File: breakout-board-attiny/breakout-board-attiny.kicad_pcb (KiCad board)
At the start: 2 copper layers, 36 x 21.5 mm, 6 parts, among them J1 Conn_01x07_Male, J2 Conn_01x07_Male, U1 ATtiny424-X

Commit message: ATtiny breakout board done
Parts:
- added D2: LED_Small, Diode_SMD:D_1206_3216Metric, F.Cu at (139.4, 97.0)
- added R1: 330, Resistor_SMD:R_1206_3216Metric, F.Cu at (139.5, 100.3)
- moved J1 0.28 mm to (146.8, 112.8)
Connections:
- net /PA1 renamed /TXD/PA1
- net /PA2 renamed /RXD/PA2
- net /PA3 renamed /XCK/PA3
- net /PA4 renamed /XDIR/PA4
- net /TX/~{RX}/PB0 renamed /SCL/XDIR/PB0
- net /XCK/PB1 renamed /SDA/XCK/PB1
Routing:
- net Net-(D2-A): track 0.00 -> 3.34 mm
- net /TxD/PB2: track 8.17 -> 11.5 mm
- added copper zone on F.Cu, net GND
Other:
- board size 36 x 21.5 mm -> 40.6 x 21.5 mm
- board text added: "PA1/TXD1"
- board text added: "PA2/RXD1"
- board text added: "PA3/XCK1"
- board text added: "PB0/XDIR0/SCL"
- board text added: "PB1/XCK0/SDA"
- board text added: "RXD0/PB3"
- board text added: "TXD0/PB2"
- board text added: "XDIR1/PA4"
- board text removed: "PA1"
- board text removed: "PA2"
- board text removed: "PA3"
- board text removed: "PA4"
- board text removed: "PB0/TX/RX"
- board text removed: "PB1/XCK"
- board text removed: "PB2/TxD"
- board text removed: "PB3/RxD"

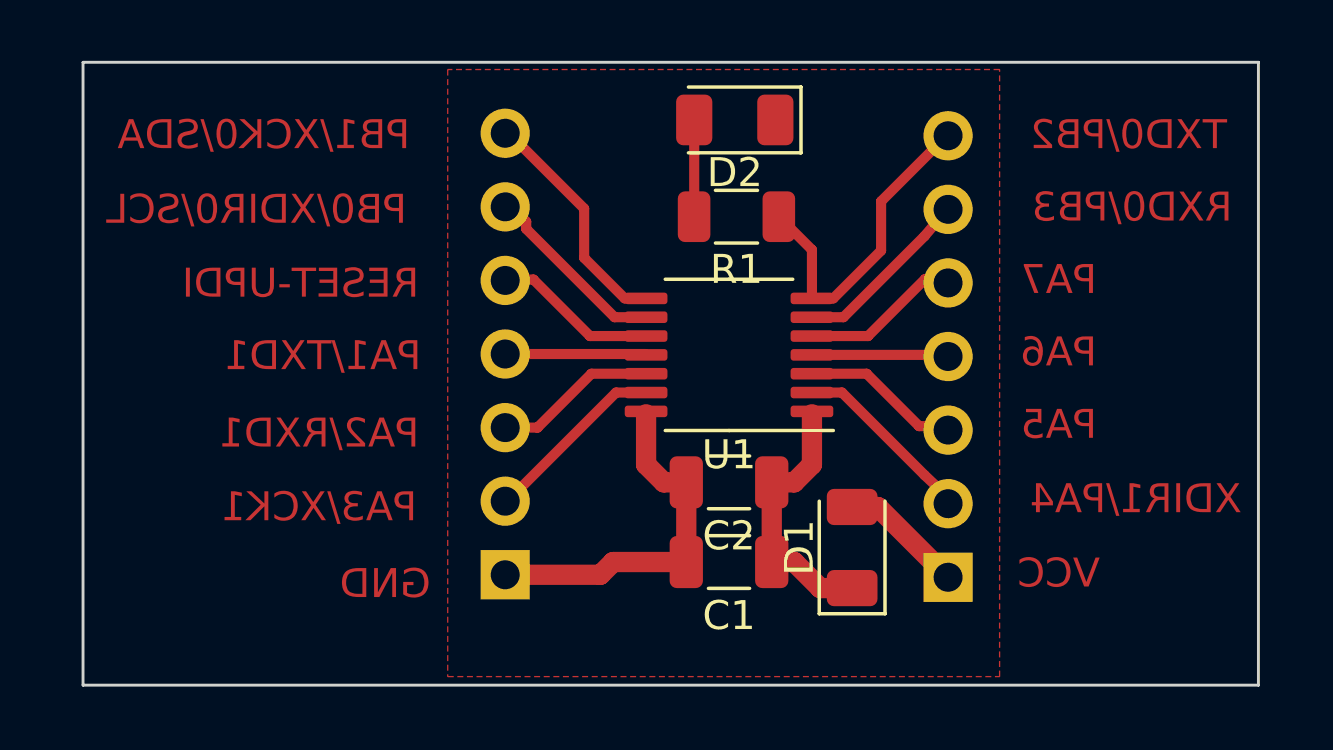
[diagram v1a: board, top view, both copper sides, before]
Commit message: ATtiny breakout board finished and ready for production
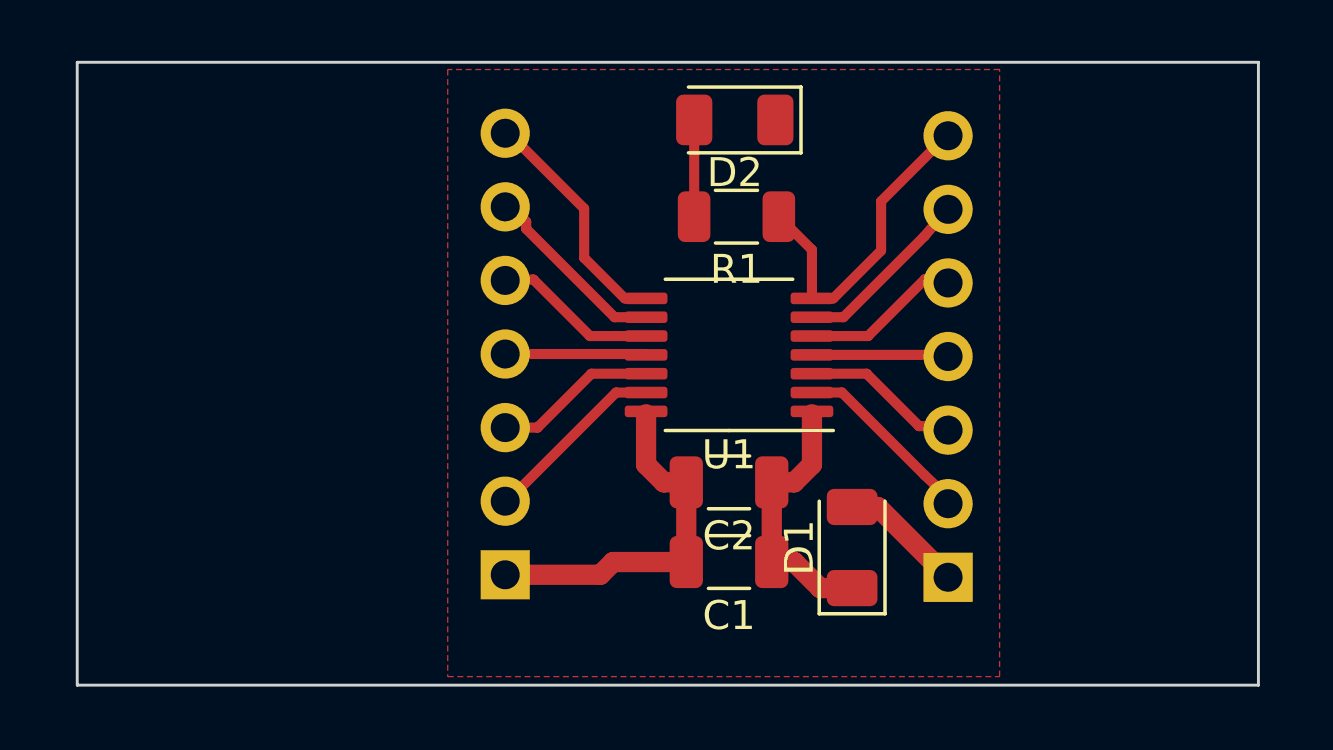
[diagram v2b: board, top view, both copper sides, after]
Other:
- board size 40.6 x 21.5 mm -> 40.8 x 21.5 mm
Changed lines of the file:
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@@
     )
   )
-  (gr_rect (start 116.952 95) (end 157.524 116.5)
+  (gr_rect (start 116.752 95) (end 157.524 116.5)
     (stroke (width 0.1) (type solid)) (fill none) (layer "Edge.Cuts"))
-  (gr_text "PA6" (at 150.627 105) (layer "F.Cu")
+  (gr_text "PA6" (at 150.627 105) (layer "B.SilkS")
     (effects (font (size 1 1) (thickness 0.15)) (justify mirror))
   )
-  (gr_text "XDIR1/PA4" (at 153.289 110.066869) (layer "F.Cu")
+  (gr_text "XDIR1/PA4" (at 153.289 110.066869) (layer "B.SilkS")
     (effects (font (size 1 1) (thickness 0.15)) (justify mirror))
   )
-  (gr_text "VCC" (at 150.627642 112.632373) (layer "F.Cu")
+  (gr_text "VCC" (at 150.627642 112.632373) (layer "B.SilkS")
     (effects (font (size 1 1) (thickness 0.15)) (justify mirror))
   )
-  (gr_text "PA7" (at 150.627 102.5) (layer "F.Cu")
+  (gr_text "PA7" (at 150.627 102.5) (layer "B.SilkS")
     (effects (font (size 1 1) (thickness 0.15)) (justify mirror))
   )
-  (gr_text "PB0/XDIR0/SCL" (at 122.936 100.076) (layer "F.Cu")
+  (gr_text "PB0/XDIR0/SCL" (at 122.936 100.076) (layer "B.SilkS")
     (effects (font (size 1 1) (thickness 0.15)) (justify mirror))
   )
-  (gr_text "PA2/RXD1" (at 125.095 107.800674) (layer "F.Cu")
+  (gr_text "PA2/RXD1" (at 125.095 107.800674) (layer "B.SilkS")
     (effects (font (size 1 1) (thickness 0.15)) (justify mirror))
   )
-  (gr_text "TXD0/PB2" (at 153.035 97.5) (layer "F.Cu")
+  (gr_text "TXD0/PB2" (at 153.035 97.5) (layer "B.SilkS")
     (effects (font (size 1 1) (thickness 0.15)) (justify mirror))
   )
-  (gr_text "PA3/XCK1" (at 125.095 110.344799) (layer "F.Cu")
+  (gr_text "PA3/XCK1" (at 125.095 110.344799) (layer "B.SilkS")
     (effects (font (size 1 1) (thickness 0.15)) (justify mirror))
   )
-  (gr_text "PB1/XCK0/SDA" (at 123.19 97.5) (layer "F.Cu")
+  (gr_text "PB1/XCK0/SDA" (at 123.19 97.5) (layer "B.SilkS")
     (effects (font (size 1 1) (thickness 0.15)) (justify mirror))
   )
-  (gr_text "PA1/TXD1\n" (at 125.222 105.128275) (layer "F.Cu")
+  (gr_text "PA1/TXD1\n" (at 125.222 105.128275) (layer "B.SilkS")
     (effects (font (size 1 1) (thickness 0.15)) (justify mirror))
   )
-  (gr_text "PA5" (at 150.627 107.5) (layer "F.Cu")
+  (gr_text "PA5" (at 150.627 107.5) (layer "B.SilkS")
     (effects (font (size 1 1) (thickness 0.15)) (justify mirror))
   )
-  (gr_text "RXD0/PB3" (at 153.162 100) (layer "F.Cu")
+  (gr_text "RXD0/PB3" (at 153.162 100) (layer "B.SilkS")
     (effects (font (size 1 1) (thickness 0.15)) (justify mirror))
   )
-  (gr_text "RESET-UPDI" (at 124.46 102.626909) (layer "F.Cu")
+  (gr_text "RESET-UPDI" (at 124.46 102.626909) (layer "B.SilkS")
     (effects (font (size 1 1) (thickness 0.15)) (justify mirror))
   )
-  (gr_text "GND" (at 127.381 112.995819) (layer "F.Cu")
+  (gr_text "GND" (at 127.381 112.995819) (layer "B.SilkS")
     (effects (font (size 1 1) (thickness 0.15)) (justify mirror))
   )

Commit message: ...
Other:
- board size 40.8 x 21.5 mm -> 19 x 19.3 mm
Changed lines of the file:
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@@
     (pad_to_mask_clearance 0)
     (pcbplotparams
-      (layerselection 0x00010fc_ffffffff)
+      (layerselection 0x0001000_7fffffff)
       (plot_on_all_layers_selection 0x0000000_00000000)
       (disableapertmacros false)
@@
       (outputformat 1)
       (mirror false)
-      (drillshape 1)
+      (drillshape 0)
       (scaleselection 1)
-      (outputdirectory "")
+      (outputdirectory "plot/")
     )
   )
@@
     (fp_line (start 1.6 0.8) (end -1.6 0.8)
       (stroke (width 0.1) (type solid)) (layer "F.Fab"))
-    (pad "1" smd roundrect (at -1.475 0 180) (size 1.15 1.8) (layers "F.Cu" "F.Paste" "F.Mask") (roundrect_rratio 0.217391)
+    (pad "1" smd roundrect (at -1.475 0 180) (size 1.15 1.8) (layers "F.Cu" "F.Paste" "F.Mask") (roundrect_rratio 0.2173913043)
       (net 1 "/sVCC") (pintype "passive"))
-    (pad "2" smd roundrect (at 1.475 0 180) (size 1.15 1.8) (layers "F.Cu" "F.Paste" "F.Mask") (roundrect_rratio 0.217391)
+    (pad "2" smd roundrect (at 1.475 0 180) (size 1.15 1.8) (layers "F.Cu" "F.Paste" "F.Mask") (roundrect_rratio 0.2173913043)
       (net 2 "GND") (pintype "passive"))
     (model "${KICAD6_3DMODEL_DIR}/Capacitor_SMD.3dshapes/C_1206_3216Metric.wrl"
@@
     (fp_line (start 1.6 0.8) (end -1.6 0.8)
       (stroke (width 0.1) (type solid)) (layer "F.Fab"))
-    (pad "1" smd roundrect (at -1.4625 0 180) (size 1.125 1.75) (layers "F.Cu" "F.Paste" "F.Mask") (roundrect_rratio 0.222222)
+    (pad "1" smd roundrect (at -1.4625 0 180) (size 1.125 1.75) (layers "F.Cu" "F.Paste" "F.Mask") (roundrect_rratio 0.2222222222)
       (net 5 "/TxD{slash}PB2") (pintype "passive"))
-    (pad "2" smd roundrect (at 1.4625 0 180) (size 1.125 1.75) (layers "F.Cu" "F.Paste" "F.Mask") (roundrect_rratio 0.222222)
+    (pad "2" smd roundrect (at 1.4625 0 180) (size 1.125 1.75) (layers "F.Cu" "F.Paste" "F.Mask") (roundrect_rratio 0.2222222222)
       (net 16 "Net-(D2-A)") (pintype "passive"))
     (model "${KICAD6_3DMODEL_DIR}/Resistor_SMD.3dshapes/R_1206_3216Metric.wrl"
@@
     (fp_line (start 1.6 0.8) (end -1.6 0.8)
       (stroke (width 0.1) (type solid)) (layer "F.Fab"))
-    (pad "1" smd roundrect (at -1.475 0 180) (size 1.15 1.8) (layers "F.Cu" "F.Paste" "F.Mask") (roundrect_rratio 0.217391)
+    (pad "1" smd roundrect (at -1.475 0 180) (size 1.15 1.8) (layers "F.Cu" "F.Paste" "F.Mask") (roundrect_rratio 0.2173913043)
       (net 1 "/sVCC") (pintype "passive"))
-    (pad "2" smd roundrect (at 1.475 0 180) (size 1.15 1.8) (layers "F.Cu" "F.Paste" "F.Mask") (roundrect_rratio 0.217391)
+    (pad "2" smd roundrect (at 1.475 0 180) (size 1.15 1.8) (layers "F.Cu" "F.Paste" "F.Mask") (roundrect_rratio 0.2173913043)
       (net 2 "GND") (pintype "passive"))
     (model "${KICAD6_3DMODEL_DIR}/Capacitor_SMD.3dshapes/C_1206_3216Metric.wrl"
@@
     )
   )
-  (gr_rect (start 116.752 95) (end 157.524 116.5)
+  (gr_rect (start 129.552 95.4) (end 148.524 114.7)
     (stroke (width 0.1) (type solid)) (fill none) (layer "Edge.Cuts"))
   (gr_text "PA6" (at 150.627 105) (layer "B.SilkS")

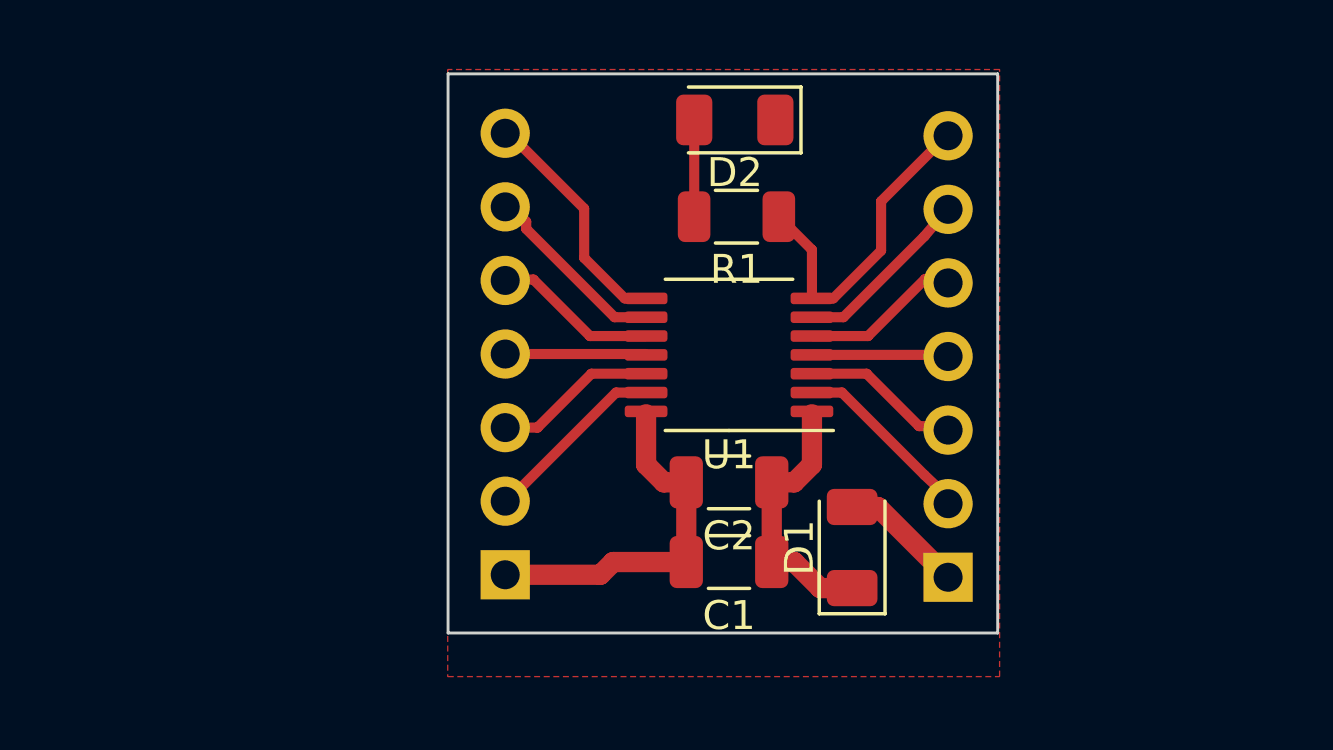
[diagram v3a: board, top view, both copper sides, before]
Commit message: changes made to attiny and display brain breakout board
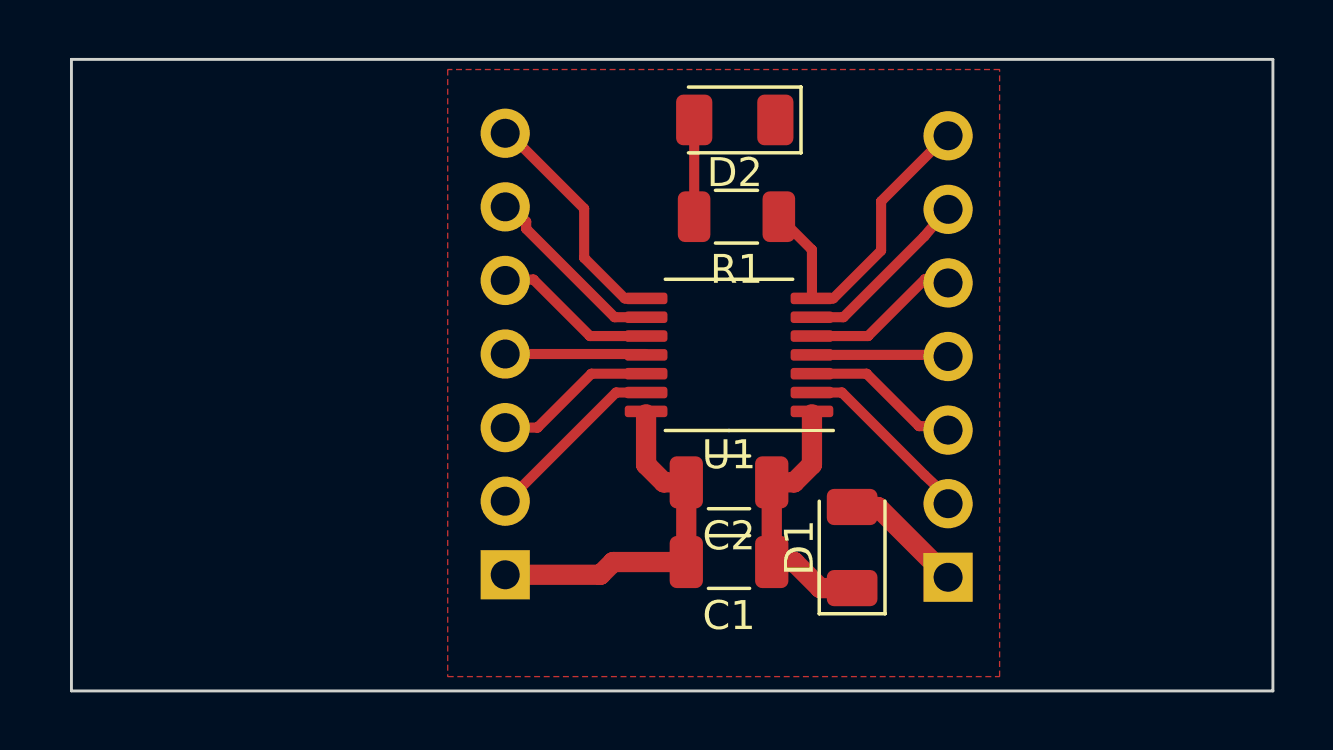
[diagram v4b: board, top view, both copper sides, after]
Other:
- board size 19 x 19.3 mm -> 41.5 x 21.8 mm
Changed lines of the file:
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@@
     )
   )
-  (gr_rect (start 129.552 95.4) (end 148.524 114.7)
+  (gr_rect (start 116.552 94.9) (end 158.024 116.7)
     (stroke (width 0.1) (type solid)) (fill none) (layer "Edge.Cuts"))
   (gr_text "PA6" (at 150.627 105) (layer "B.SilkS")
